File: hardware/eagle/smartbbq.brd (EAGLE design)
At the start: 100 x 76.2 mm, 59 parts, among them J1 MJ_2523_SMT, J2 MJ_2523_SMT, J3 MJ_2523_SMT, J4 MJ_2523_SMT, J5 5.5od/2.1id, J6 5.5od/2.5id, J7 5.5od/2.5id, J8 +, J9 +, P1 CMT_1603_SMT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

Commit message: rev0.1 of board
rev0.1 of board and minor schematic edits
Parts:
- added U$1: (no value), SparkFun-Aesthetics:OSHW-LOGO-L
- moved F1 10.4 mm to (84.0, 22.0), turned to 180 degrees
- moved C6 9.00 mm to (94.0, 21.0), turned to 180 degrees
- moved C7 3.00 mm to (85.0, 32.0)
- moved D1 3.00 mm to (85.0, 28.0)
- moved R1 2.42 mm to (3.10, 19.9)
- moved R2 2.42 mm to (14.1, 19.9)
- moved R3 2.42 mm to (25.1, 19.9)
- moved R4 2.42 mm to (36.1, 19.9)
- moved R5 2.42 mm to (10.9, 19.9)
- moved R6 2.42 mm to (21.9, 19.9)
- moved R7 2.42 mm to (32.9, 19.9)
- moved R8 2.42 mm to (43.9, 19.9)
- moved C1 2.40 mm to (8.30, 19.9)
- moved C2 2.40 mm to (19.3, 19.9)
- moved C3 2.40 mm to (30.3, 19.9)
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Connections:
- net +12V: now also J8.1, J9.1; no longer J8.2, J9.2
- net N$30: now also J9.2; no longer J9.1
- net N$32: now also J8.2; no longer J8.1
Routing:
- net +3V3: track 105.0 -> 134.6 mm, vias 2 -> 3
- net N$29: track 106.8 -> 85.5 mm, vias 1 -> 2
- net A0: track 54.1 -> 35.6 mm
- net N$21: track 41.9 -> 59.4 mm
- net N$23: track 52.6 -> 39.2 mm
- net N$35: track 12.6 -> 25.8 mm
- net N$7: track 66.2 -> 55.0 mm, vias 1 -> 3
- net N$32: track 38.5 -> 27.3 mm, vias 1 -> 2
- net N$27: track 42.8 -> 53.9 mm, vias 2 -> 1
- net N$25: track 56.4 -> 48.9 mm
- net N$38: track 22.2 -> 15.7 mm
- net N$14: track 52.0 -> 57.8 mm
- net N$22: track 45.1 -> 39.4 mm, vias 1 -> 2
- net +12V: track 94.3 -> 99.8 mm
- net FAN1: track 34.5 -> 29.2 mm
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- removed copper zone on layer 16, net GND
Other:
- board text added: "https://github.com/engirati/smart-bbq"
- board text added: "rev0.1"
- board text added: "smartbbq"

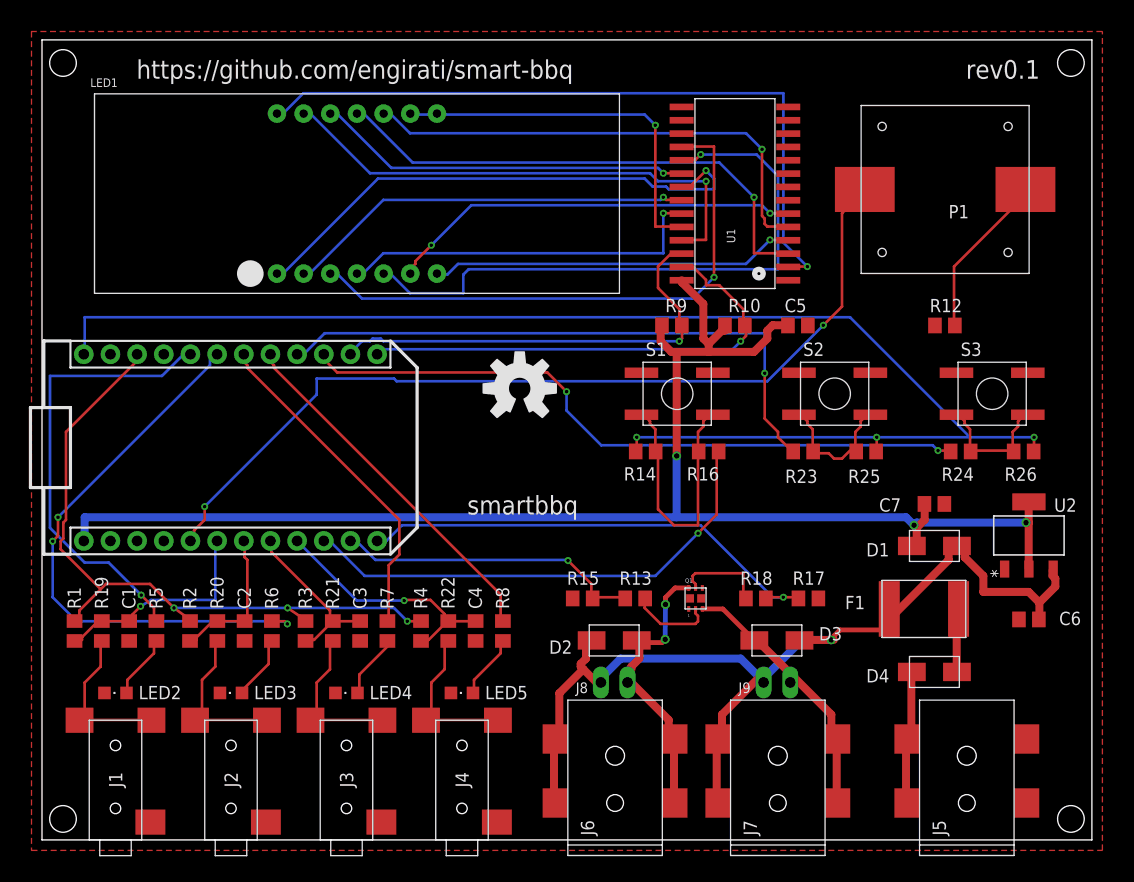
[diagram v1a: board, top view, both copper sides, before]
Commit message: Heatsink pads added
Added larger pads to act as a heatsink for voltage regulator and mosfet.
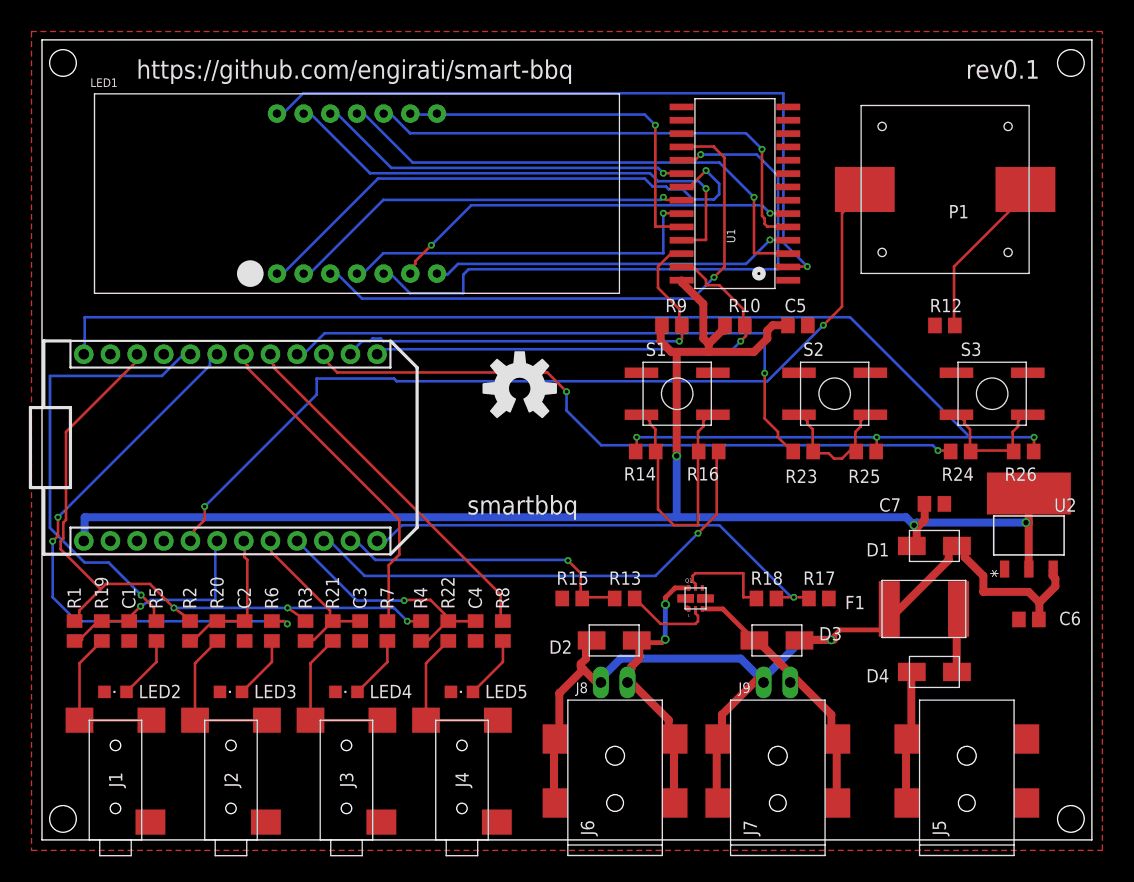
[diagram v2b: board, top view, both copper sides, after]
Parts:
- moved R13 1.00 mm to (55.5, 23.0)
- moved R15 1.00 mm to (50.5, 23.0)
- moved R17 1.00 mm to (74.0, 23.0)
- moved R18 1.00 mm to (69.0, 23.0)
- moved LED2 0.10 mm to (7.00, 14.1)
- moved LED3 0.10 mm to (18.0, 14.1)
- moved LED4 0.10 mm to (29.0, 14.1)
- moved LED5 0.10 mm to (40.0, 14.1)
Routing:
- net N$24: track 51.1 -> 52.9 mm
- net N$31: track 8.74 -> 9.74 mm
- net FAN2: track 45.3 -> 46.3 mm
- net GND: track 0.00 -> 0.94 mm
- net N$27: track 53.9 -> 54.7 mm
